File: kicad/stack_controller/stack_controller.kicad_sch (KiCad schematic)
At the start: 30 parts

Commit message: Improved timing
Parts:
- removed U13: (no value), Package_DIP:DIP-14_W7.62mm, symbol custom_symbol_lib:quad_and
- removed U19: (no value), Package_DIP:DIP-14_W7.62mm, symbol custom_symbol_lib:6xNOT
- removed U24, U9: (no value), Package_DIP:DIP-14_W7.62mm, symbol custom_symbol_lib:quad_OR
- removed U25, U27: (no value), Package_DIP:DIP-20_W7.62mm, symbol custom_symbol_lib:rising_edge_8_bit_latch
- added U13, U31: ~, Package_DIP:DIP-14_W7.62mm, symbol custom_symbol_lib:6xNOT
- added U19, U24: ~, Package_DIP:DIP-14_W7.62mm, symbol custom_symbol_lib:quad_and
- added U25, U27: ~, Package_DIP:DIP-14_W7.62mm, symbol custom_symbol_lib:quad_OR
- added U9: ~, Package_DIP:DIP-20_W7.62mm, symbol custom_symbol_lib:rising_edge_8_bit_latch
- U1, U10, U11, U12, U14, U15, U16, U17, U18, U2, U20, U21, U22, U23, U26, U28, U29, U3, U30, U4, U5, U6, U7, U8: value (none) -> ~
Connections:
- net at U1.6 (B0), U1.7 (C_IN), U1.8 (GND)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: now also U19.7 (GND), U9.1 (OE#), U9.10 (GND); no longer U28.7 (GND)
- net at U20.1 (S), U21.1 (S), U22.1 (S)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: no longer U26.14 (Q5)
- net at U26.18 (Q1): now also U26.19 (Q0), U28.10 (4A), U31.1 (I0), U9.2 (D0)
- net at U26.2 (D0): now also U28.3 (1Q)
- net at U1.16 (V+), U10.28 (V+), U11.28 (V+)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: now also U19.14 (V+); no longer U26.20 (V+), U28.14 (V+)
- net at U26.3 (D1): now also U9.19 (Q0)
- net at U5.4 (WRITE_0): now also U25.2 (0B)
- net at U28.1 (1A): now also U19.2 (1B), U19.4 (2A), U25.3 (Q0)
- net at U5.5 (WRITE_1): now also U25.1 (0A)
- net at U23.12 (Q3): now also U11.20 (CE#), U13.1 (I0)
- net at U5.20 (FAULT): now also U25.11 (Q3)
- net at U10.22 (OE#), U11.22 (OE#): now also U13.4 (O1)
- net at U10.27 (WE#), U11.27 (WE#): now also U13.6 (O2)
- net at U6.11 (CLK), U7.11 (CLK): no longer U28.3 (1Q)
- net at U28.8 (4Q): now also U27.13 (3B)
- net at U28.9 (4B): now also U26.11 (CLK), U5.9 (CLK_B)
- net at U10.20 (CE#): now also U13.2 (O0)
- net at U30.1 (OE#): now also U19.11 (3Q)
- new net: U13.8 (03), U19.1 (1A), U19.13 (3A)
- new net: U19.12 (3B), U19.5 (2B)
- new net: U13.3 (I1), U19.3 (1Q)
- new net: U13.9 (I3), U19.6 (2Q)
- new net: U5.8 (CLK_A), U9.11 (CLK)
- new net: U28.2 (1B), U31.2 (O0)
- now unconnected: U28.12 (3B), U28.5 (2B)
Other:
- note added: "<- Memory bus"
- note added: "Fault"
- note added: "Input latch"
- note added: "Mem bus protection Simultaneous read & input latch OE protection"
- note added: "Output latch"
- note added: "Pointer adder input latch CLK Pointer inc (0) / dec (1) select Pointer latch CLK ToS (0) / offset (1) select"
- note added: "Read (mem output enable) Write Input latch CLK Input latch output enable Output latch CLK Output latch output enable"
- note removed: "<- Possible pointer decrement"
- note removed: "<- Push or Pop (load new pointer)"
- note removed: "<- Push or offset write (Write SRAM)"
- note removed: "<- Save bus value"
- note removed: "<- Select offset"
- note removed: "Inc (0) or Dec (1)"
- note removed: "Load new value"
- note removed: "Memory chip control"
- note removed: "Read"
- note removed: "Select offset"
- note removed: "Write"

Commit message: Possibly final design of stack controller
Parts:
- added U32: ~, Connector_PinHeader_2.54mm:PinHeader_1x08_P2.54mm_Vertical, symbol custom_symbol_lib:connector_8_bit
- added U33: ~, Connector_PinHeader_2.54mm:PinHeader_1x16_P2.54mm_Vertical, symbol custom_symbol_lib:connector_16_bit
- added U34, U35, U36, U37, U38, U39, U40, U41, U42, U43, U44, U45, U46: ~, custom_footprint_library:jumper, symbol custom_symbol_lib:jumper
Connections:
- net at U25.1 (0A), U5.5 (WRITE_1): now also U27.5 (1A)
- net at U25.10 (Q2): now also U24.13 (3A), U9.3 (D1)
- net at U25.12 (3A): now also U45.3 (OUT)
- net at U25.13 (3B): now also U46.3 (OUT)
- net at U25.14 (V+): now also U1.16 (V+), U1.6 (B0), U10.28 (V+), U11.28 (V+), U12.20 (V+), U13.14 (V+), U14.16 (V+), U15.16 (V+), U16.11 (B3), U16.15 (B2), U16.16 (V+), U16.2 (B1), U16.6 (B0), U17.11 (B3), U17.15 (B2), U17.16 (V+), U17.2 (B1), U17.6 (B0), U18.20 (V+), U19.14 (V+), U2.16 (V+), U20.16 (V+), U21.16 (V+), U22.16 (V+), U23.16 (V+), U24.14 (V+), U26.20 (V+), U27.1 (0A), U27.14 (V+), U27.2 (0B), U28.14 (V+), U29.20 (V+), U3.16 (V+), U30.20 (V+), U31.14 (V+), U4.16 (V+), U5.10 (V+), U6.20 (V+), U7.20 (V+), U8.20 (V+), U9.20 (V+)
- net at U25.2 (0B), U5.4 (WRITE_0): now also U24.2 (1B), U35.1 (IN)
- net at U25.3 (Q0), U28.1 (1A): now also U39.1 (IN); no longer U19.2 (1B), U19.4 (2A)
- net at U25.5 (1A): now also U1.7 (C_IN), U1.8 (GND), U10.14 (GND), U11.14 (GND), U12.1 (OE#), U12.10 (GND), U13.7 (GND), U14.7 (C_IN), U14.8 (GND), U15.8 (GND), U16.8 (GND), U17.8 (GND), U18.1 (OE#), U18.10 (GND), U19.7 (GND), U2.8 (GND), U20.15 (OE#), U20.8 (GND), U21.15 (OE#), U21.8 (GND), U22.15 (OE#), U22.8 (GND), U23.15 (OE#), U23.8 (GND), U24.7 (GND), U25.6 (1B), U25.7 (GND), U26.1 (OE#), U26.10 (GND), U26.9 (D7), U27.7 (GND), U28.7 (GND), U29.10 (GND), U3.8 (GND), U30.10 (GND), U31.11 (I4), U31.13 (I5), U31.3 (I1), U31.5 (I2), U31.7 (GND), U31.9 (I3), U4.8 (GND), U5.11 (GND), U6.1 (OE#), U6.10 (GND), U7.1 (OE#), U7.10 (GND), U8.1 (OE#), U8.10 (GND), U9.1 (OE#), U9.10 (GND), U34.2 (GND), U35.2 (GND), U36.2 (GND), U37.2 (GND), U38.2 (GND), U39.2 (GND), U40.2 (GND), U41.2 (GND), U42.2 (GND), U43.2 (GND), U44.2 (GND), U45.2 (GND), U46.2 (GND)
- net at U25.8 (2A): now also U5.2 (READ_1), U9.8 (D6)
- net at U25.9 (2B): now also U5.1 (READ_0), U9.6 (D4)
- net at U24.1 (1A): now also U28.11 (3Q)
- net at U24.10 (4A): now also U9.14 (Q5)
- net at U24.11 (3Q): now also U27.12 (3A), U41.1 (IN)
- net at U24.12 (3B): now also U24.4 (2A), U24.9 (4B), U28.5 (2B), U5.8 (CLK_A), U9.11 (CLK)
- net at U24.3 (1Q): now also U27.9 (2B)
- net at U24.5 (2B): now also U9.16 (Q3)
- net at U24.6 (2Q): now also U40.1 (IN)
- net at U24.8 (4Q): now also U27.8 (2A)
- net at U12.11 (CLK), U8.11 (CLK): now also U19.9 (4B), U34.3 (OUT)
- net at U1.11 (B3), U1.15 (B2), U1.2 (B1)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: now also U35.3 (OUT)
- net at U20.1 (S), U21.1 (S), U22.1 (S)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: now also U37.3 (OUT)
- net at U10.7 (A3), U11.7 (A3), U20.12 (Q3): now also U33.4 (3)
- net at U10.10 (A0), U11.10 (A0), U20.4 (Q0): now also U33.1 (0)
- net at U10.9 (A1), U11.9 (A1), U20.7 (Q1): now also U33.2 (1)
- net at U10.8 (A2), U11.8 (A2), U20.9 (Q2): now also U33.3 (2)
- net at U19.10 (4A): now also U6.11 (CLK), U7.11 (CLK), U36.3 (OUT)
- net at U19.11 (3Q): now also U13.11 (I4); no longer U30.1 (OE#)
- net at U19.12 (3B), U19.5 (2B): now also U42.3 (OUT)
- net at U13.9 (I3), U19.6 (2Q): now also U45.1 (IN)
- net at U19.8 (4Q): now also U46.1 (IN)
- net at U5.3 (READ_2): now also U28.4 (2A); no longer U18.11 (CLK)
- net at U5.7 (READ_READY): now also U26.19 (Q0), U28.10 (4A), U31.1 (I0), U9.2 (D0), U44.1 (IN)
- net at U26.11 (CLK), U28.9 (4B), U5.9 (CLK_B): now also U28.13 (3A)
- net at U11.20 (CE#), U13.1 (I0), U23.12 (Q3): now also U33.16 (15)
- net at U13.10 (O4): now also U30.1 (OE#)
- net at U13.12 (O5): now also U29.1 (OE#)
- net at U13.13 (I5): now also U44.3 (OUT)
- net at U13.5 (I2): now also U40.3 (OUT)
- net at U10.1 (A14), U11.1 (A14), U23.9 (Q2): now also U33.15 (14)
- net at U10.11 (D0), U11.11 (D0), U29.2 (D0)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: now also U32.1 (0)
- net at U10.12 (D1), U11.12 (D1), U29.3 (D1)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: now also U32.2 (1)
- net at U10.13 (D2), U11.13 (D2), U29.4 (D2)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: now also U32.3 (2)
- net at U10.15 (D3), U11.15 (D3), U29.5 (D3)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: now also U32.4 (3)
- net at U10.16 (D4), U11.16 (D4), U29.6 (D4)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: now also U32.5 (4)
- net at U10.17 (D5), U11.17 (D5), U29.7 (D5)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: now also U32.6 (5)
- net at U10.18 (D6), U11.18 (D6), U29.8 (D6)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: now also U32.7 (6)
- net at U10.19 (D7), U11.19 (D7), U29.9 (D7)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: now also U32.8 (7)
- net at U10.2 (A12), U11.2 (A12), U23.4 (Q0): now also U33.13 (12)
- net at U10.21 (A10), U11.21 (A10), U22.9 (Q2): now also U33.11 (10)
- net at U10.23 (A11), U11.23 (A11), U22.12 (Q3): now also U33.12 (11)
- net at U10.24 (A9), U11.24 (A9), U22.7 (Q1): now also U33.10 (9)
- net at U10.25 (A8), U11.25 (A8), U22.4 (Q0): now also U33.9 (8)
- net at U10.26 (A13), U11.26 (A13), U23.7 (Q1): now also U33.14 (13)
- net at U10.3 (A7), U11.3 (A7), U21.12 (Q3): now also U33.8 (7)
- net at U10.4 (A6), U11.4 (A6), U21.9 (Q2): now also U33.7 (6)
- net at U10.5 (A5), U11.5 (A5), U21.7 (Q1): now also U33.6 (5)
- net at U10.6 (A4), U11.6 (A4), U21.4 (Q0): now also U33.5 (4)
- net at U26.13 (Q6): now also U27.6 (1B)
- net at U26.14 (Q5): now also U9.9 (D7)
- net at U26.15 (Q4): now also U9.7 (D5)
- net at U26.16 (Q3): now also U9.5 (D3), U42.1 (IN)
- net at U26.17 (Q2): now also U9.4 (D2)
- net at U26.4 (D2): now also U9.18 (Q1)
- net at U26.5 (D3): now also U9.17 (Q2)
- net at U26.6 (D4): now also U9.15 (Q4)
- net at U26.7 (D5): now also U9.13 (Q6)
- net at U26.8 (D6): now also U9.12 (Q7)
- net at U27.10 (Q2): now also U36.1 (IN)
- net at U27.11 (Q3): now also U34.1 (IN)
- net at U27.13 (3B), U28.8 (4Q): now also U43.1 (IN)
- net at U27.4 (Q1): now also U37.1 (IN)
- net at U29.11 (CLK): now also U43.3 (OUT)
- net at U30.11 (CLK): now also U41.3 (OUT)
- net at U28.12 (3B): now also U26.18 (Q1)
- net at U28.6 (2Q): now also U38.1 (IN)
- new net: U19.2 (1B), U19.4 (2A), U39.3 (OUT)
- new net: U18.11 (CLK), U38.3 (OUT)
- no-connect marks 2 -> 11
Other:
- note added: "A CLK"
- note added: "B CLK"
- note added: "Memory & memory control"
- note added: "Memory bus"
- note added: "Pointer adder input latch CLK Pointer inc (0) / dec (1) select Pointer latch CLK ToS (0) / offset (1) select Offset latch CLK"
- note added: "Pointer math"
- note added: "Timing control logic"
- note added: "ToS or offset selectors"
- note added: "^ Latch for storing stack offset (Must be 2's complement)"
- note removed: "<- Memory bus"
- note removed: "Pointer adder input latch CLK Pointer inc (0) / dec (1) select Pointer latch CLK ToS (0) / offset (1) select"
- title: (none) -> Stack control unit
- moved on the sheet: U1, U10, U11, U12, U13, U14, U15, U16, U17, U18, U19, U2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

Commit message: kicad stuff and timing
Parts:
- U5: footprint custom_footprint_library:bus_connector -> Connector_PinHeader_2.54mm:PinHeader_1x22_P2.54mm_Vertical
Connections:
- net at U1.7 (C_IN), U1.8 (GND), U10.14 (GND)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: now also U5.13 (GND); no longer U5.11 (GND)
- net at U25.1 (0A), U27.5 (1A): now also U5.6 (WRITE_1); no longer U5.5 (WRITE_1)
- net at U25.11 (Q3): now also U5.22 (FAULT); no longer U5.20 (FAULT)
- net at U1.16 (V+), U1.6 (B0), U10.28 (V+)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: now also U5.12 (V+); no longer U5.10 (V+)
- net at U24.2 (1B), U25.2 (0B), U35.1 (IN): now also U5.5 (WRITE_0); no longer U5.4 (WRITE_0)
- net at U24.12 (3B), U24.4 (2A), U24.9 (4B)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: now also U5.10 (CLK_A); no longer U5.8 (CLK_A)
- net at U18.2 (D0), U29.19 (Q0), U30.2 (D0): now also U5.14 (D0); no longer U5.12 (D0)
- net at U18.3 (D1), U29.18 (Q1), U30.3 (D1): now also U5.15 (D1); no longer U5.13 (D1)
- net at U18.4 (D2), U29.17 (Q2), U30.4 (D2): now also U5.16 (D2); no longer U5.14 (D2)
- net at U18.5 (D3), U29.16 (Q3), U30.5 (D3): now also U5.17 (D3); no longer U5.15 (D3)
- net at U18.6 (D4), U29.15 (Q4), U30.6 (D4): now also U5.18 (D4); no longer U5.16 (D4)
- net at U18.7 (D5), U29.14 (Q5), U30.7 (D5): now also U5.19 (D5); no longer U5.17 (D5)
- net at U18.8 (D6), U29.13 (Q6), U30.8 (D6): now also U5.20 (D6); no longer U5.18 (D6)
- net at U18.9 (D7), U29.12 (Q7), U30.9 (D7): now also U5.21 (D7); no longer U5.19 (D7)
- net at U26.19 (Q0), U28.10 (4A), U31.1 (I0)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: now also U5.9 (READ_READY); no longer U5.7 (READ_READY)
- net at U26.11 (CLK), U28.13 (3A), U28.9 (4B): now also U5.11 (CLK_B); no longer U5.9 (CLK_B)
- no-connect marks 11 -> 13

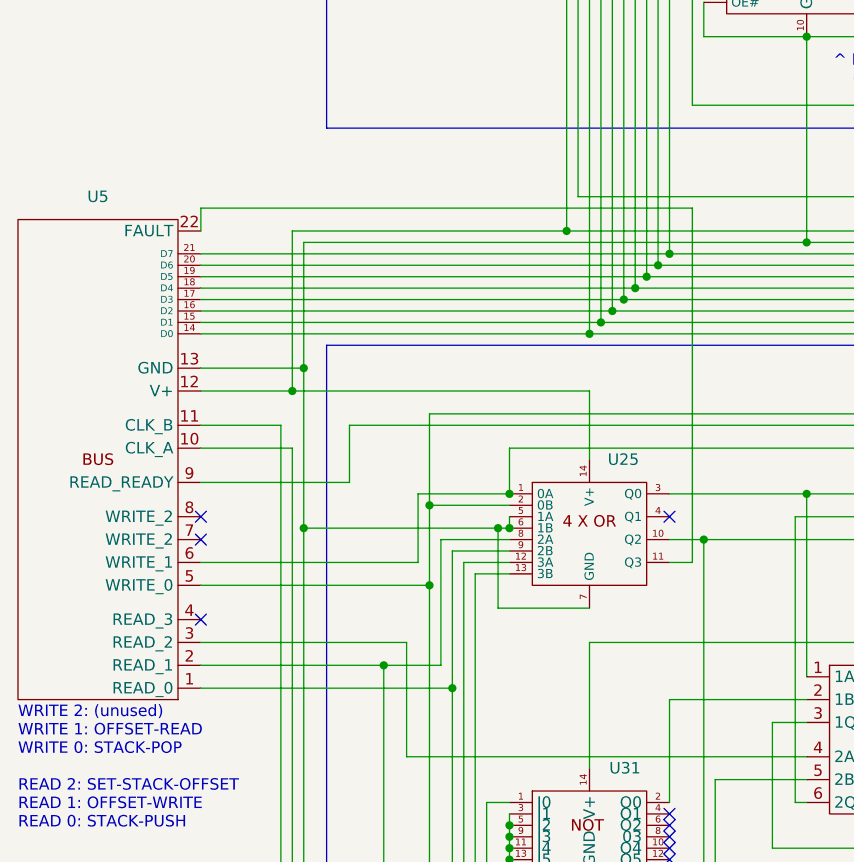
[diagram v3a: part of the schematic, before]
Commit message: Finished schematic for motherboard
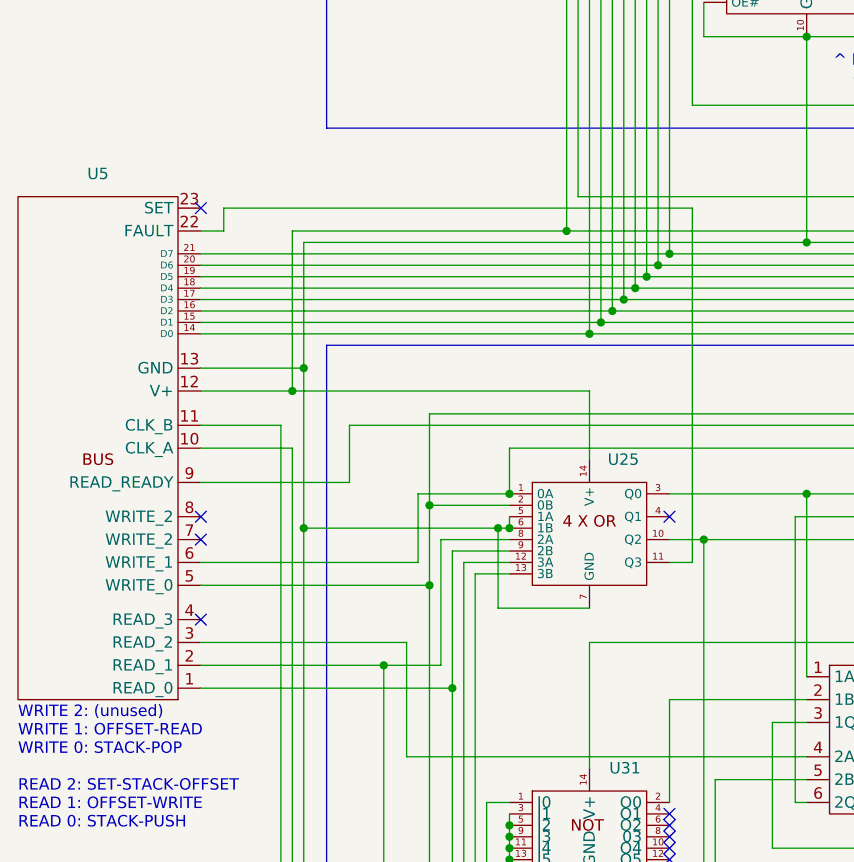
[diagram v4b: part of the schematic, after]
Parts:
- U1, U10, U11, U12, U13, U14, U15, U16, U17, U18, U19, U2, U20, U21, U22, U23, U24, U25, U26, U27, U28, U29, U3, U30, U31, U32, U33, U34, U35, U36, U37, U38, U39, U4, U40, U41, U42, U43, U44, U45, U46, U6, U7, U8, U9: value ~ -> (none)
- U5: value ~ -> (none); footprint Connector_PinHeader_2.54mm:PinHeader_1x22_P2.54mm_Vertical -> Connector_PinHeader_2.54mm:PinHeader_1x23_P2.54mm_Vertical
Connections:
- no-connect marks 13 -> 14
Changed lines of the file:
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@@
 	)
 	(no_connect
+		(at 115.57 210.82)
+	)
+	(no_connect
 		(at 167.64 281.94)
 	)
@@
 	(wire
 		(pts
-			(xy 115.57 210.82) (xy 115.57 213.36)
-		)
-		(stroke
-			(width 0)
-			(type default)
-		)
-	)
-	(wire
-		(pts
 			(xy 289.56 294.64) (xy 287.02 294.64)
 		)
@@
 	(wire
 		(pts
+			(xy 115.57 213.36) (xy 118.11 213.36)
+		)
+		(stroke
+			(width 0)
+			(type default)
+		)
+	)
+	(wire
+		(pts
 			(xy 448.31 163.83) (xy 435.61 163.83)
 		)
@@
 	(wire
 		(pts
+			(xy 118.11 213.36) (xy 118.11 210.82)
+		)
+		(stroke
+			(width 0)
+			(type default)
+		)
+	)
+	(wire
+		(pts
 			(xy 166.37 217.17) (xy 490.22 217.17)
 		)
@@
 	(wire
 		(pts
-			(xy 170.18 210.82) (xy 115.57 210.82)
+			(xy 170.18 210.82) (xy 118.11 210.82)
 		)
 		(stroke
@@
 			)
 		)
-		(property "Value" "~"
+		(property "Value" ""
 			(at 369.57 265.43 0)
 			(effects
@@
 			)
 		)
-		(property "Value" "~"
+		(property "Value" ""
 			(at 158.75 252.73 0)
 			(effects
@@
 			)
 		)
-		(property "Value" "~"
+		(property "Value" ""
 			(at 354.33 314.96 0)
 			(effects
@@
 			)
 		)
-		(property "Value" "~"
+		(property "Value" ""
 			(at 369.57 257.81 0)
 			(effects
@@
 			)
 		)
-		(property "Value" "~"
+		(property "Value" ""
 			(at 344.17 237.49 0)
 			(effects
@@
 			)
 		)
-		(property "Value" "~"
+		(property "Value" ""
 			(at 279.4 294.64 0)
 			(effects
@@
 			)
 		)
-		(property "Value" "~"
+		(property "Value" ""
 			(at 369.57 261.62 0)
 			(effects
@@
 			)
 		)
-		(property "Value" "~"
+		(property "Value" ""
 			(at 170.18 125.73 0)
 			(effects
@@
 			)
 		)
-		(property "Value" "~"
+		(property "Value" ""
 			(at 195.58 127 0)
 			(effects
@@
 			)
 		)
-		(property "Value" "~"
+		(property "Value" ""
 			(at 414.02 121.92 0)
 			(effects
@@
 			)
 		)
-		(property "Value" "~"
+		(property "Value" ""
 			(at 455.93 115.57 0)
 			(effects
@@
 			)
 		)
-		(property "Value" "~"
+		(property "Value" ""
 			(at 354.33 311.15 0)
 			(effects
@@
 			)
 		)
-		(property "Value" "~"
+		(property "Value" ""
 			(at 358.14 179.07 0)
 			(effects
@@
 			)
 		)
-		(property "Value" "~"
+		(property "Value" ""
 			(at 419.1 243.84 0)
 			(effects
@@
 			)
 		)
-		(property "Value" "~"
+		(property "Value" ""
 			(at 220.98 116.84 0)
 			(effects
@@
 		(fields_autoplaced yes)
 		(property "Reference" "U5"
-			(at 104.14 209.55 0)
+			(at 104.14 207.01 0)
 			(effects
 				(font
@@
 			)
 		)
-		(property "Value" "~"
+		(property "Value" ""
 			(at 113.03 246.38 0)
 			(effects
@@
 			)
 		)
-		(property "Footprint" "Connector_PinHeader_2.54mm:PinHeader_1x22_P2.54mm_Vertical"
-			(at 104.394 209.296 0)
+		(property "Footprint" "Connector_PinHeader_2.54mm:PinHeader_1x23_P2.54mm_Vertical"
+			(at 104.394 206.248 0)
 			(effects
 				(font
@@
 		(pin "22"
 		)
+		(pin "23"
+		)
 		(instances
 			(project "stack_controller"
@@
 			)
 		)
-		(property "Value" "~"
+		(property "Value" ""
 			(at 344.17 233.68 0)
 			(effects
@@
 			)
 		)
-		(property "Value" "~"
+		(property "Value" ""
 			(at 440.69 198.12 0)
 			(effects
@@
 			)
 		)
-		(property "Value" "~"
+		(property "Value" ""
 			(at 246.38 106.68 0)
 			(effects
@@
 			)
 		)
-		(property "Value" "~"
+		(property "Value" ""
 			(at 419.1 185.42 0)
 			(effects
@@
 			)
 		)
-		(property "Value" "~"
+		(property "Value" ""
 			(at 344.17 245.11 0)
 			(effects
@@
 			)
 		)
-		(property "Value" "~"
+		(property "Value" ""
 			(at 271.78 96.52 0)
 			(effects
@@
 			)
 		)
-		(property "Value" "~"
+		(property "Value" ""
 			(at 231.14 327.66 0)
 			(effects
@@
 			)
 		)
-		(property "Value" "~"
+		(property "Value" ""
 			(at 204.47 175.26 0)
 			(effects
@@
 			)
 		)
-		(property "Value" "~"
+		(property "Value" ""
 			(at 238.76 175.26 0)
 			(effects
@@
 			)
 		)
-		(property "Value" "~"
+		(property "Value" ""
 			(at 344.17 229.87 0)
 			(effects
@@
 			)
 		)
-		(property "Value" "~"
+		(property "Value" ""
 			(at 356.87 158.75 0)
 			(effects
@@
 			)
 		)
-		(property "Value" "~"
+		(property "Value" ""
 			(at 344.17 241.3 0)
 			(effects
@@
 			)
 		)
-		(property "Value" "~"
+		(property "Value" ""
 			(at 250.19 137.16 0)
 			(effects
@@
 			)
 		)
-		(property "Value" "~"
+		(property "Value" ""
 			(at 180.34 194.31 0)
 			(effects
@@
 			)
 		)
-		(property "Value" "~"
+		(property "Value" ""
 			(at 260.35 267.97 0)
 			(effects
@@
 			)
 		)
-		(property "Value" "~"
+		(property "Value" ""
 			(at 355.6 138.43 0)
 			(effects
@@
 			)
 		)
-		(property "Value" "~"
+		(property "Value" ""
 			(at 156.21 105.41 0)
 			(effects
@@
 			)
 		)
-		(property "Value" "~"
+		(property "Value" ""
 			(at 369.57 273.05 0)
 			(effects
@@
 			)
 		)
-		(property "Value" "~"
+		(property "Value" ""
 			(at 369.57 276.86 0)
 			(effects
@@
 			)
 		)
-		(property "Value" "~"
+		(property "Value" ""
 			(at 273.05 175.26 0)
 			(effects
@@
 			)
 		)
-		(property "Value" "~"
+		(property "Value" ""
 			(at 298.45 105.41 0)
 			(effects
@@
 			)
 		)
-		(property "Value" "~"
+		(property "Value" ""
 			(at 471.17 180.34 0)
 			(effects
@@
 			)
 		)
-		(property "Value" "~"
+		(property "Value" ""
 			(at 354.33 118.11 0)
 			(effects
@@
 			)
 		)
-		(property "Value" "~"
+		(property "Value" ""
 			(at 419.1 157.48 0)
 			(effects
@@
 			)
 		)
-		(property "Value" "~"
+		(property "Value" ""
 			(at 369.57 269.24 0)
 			(effects
@@
 			)
 		)
-		(property "Value" "~"
+		(property "Value" ""
 			(at 476.25 152.4 0)
 			(effects
@@
 			)
 		)
-		(property "Value" "~"
+		(property "Value" ""
 			(at 156.21 280.67 0)
 			(effects
@@
 			)
 		)
-		(property "Value" "~"
+		(property "Value" ""
 			(at 308.61 175.26 0)
 			(effects
@@
 			)
 		)
-		(property "Value" "~"
+		(property "Value" ""
 			(at 182.88 327.66 0)
 			(effects
@@
 			)
 		)
-		(property "Value" "~"
+		(property "Value" ""
 			(at 193.04 271.78 0)
 			(effects

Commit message: stuff
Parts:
- added U47: ~, Package_DIP:DIP-14_W7.62mm, symbol custom_symbol_lib:quad_and
- U1, U10, U11, U12, U13, U14, U15, U16, U17, U18, U19, U2, U20, U21, U22, U23, U24, U25, U26, U27, U28, U29, U3, U30, U31, U32, U33, U34, U35, U36, U37, U38, U39, U4, U40, U41, U42, U43, U44, U45, U46, U5, U6, U7, U8, U9: value (none) -> ~
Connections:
- net at U1.7 (C_IN), U1.8 (GND), U10.14 (GND)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: now also U47.10 (4A), U47.12 (3B), U47.13 (3A), U47.4 (2A), U47.5 (2B), U47.7 (GND), U47.9 (4B)
- net at U1.16 (V+), U1.6 (B0), U10.28 (V+)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: now also U47.14 (V+)
- net at U5.23 (ENABLE): now also U47.2 (1B)
- net at U26.19 (Q0), U28.10 (4A), U31.1 (I0)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: now also U47.1 (1A); no longer U44.1 (IN)
- new net: U44.1 (IN), U47.3 (1Q)
- no-connect marks 14 -> 16
